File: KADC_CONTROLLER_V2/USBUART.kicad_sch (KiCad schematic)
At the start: 11 parts, among them J14 ZX62D-B-5P830, U10 PUSB3FR4Z, U9 FT230XQ-R

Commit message: many updates
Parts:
- added C159, C161, C174, C175, C176, C181, C182, C183, C184, C185, C26, C84, C86, C87: 0.1u, symbol Device:C_Small
- added C160, C177, C82, C83: 10u, symbol Device:C_Small
- added C186: 2.2u, symbol Device:C_Small
- added C2, C27, C3, C70, C71: 22u, symbol Device:C_Small
- added J1, J7: GSB311231HR, GSB311231HR_AMP, symbol GSB311231HR:GSB311231HR
- added R11: 12k, Resistor_SMD:R_0603_1608Metric, symbol Device:R_Small_US
- added R12, R13: 200k, Resistor_SMD:R_0603_1608Metric, symbol Device:R_Small_US
- added R159, R160: DNP, Resistor_SMD:R_0603_1608Metric, symbol Device:R_Small_US
- added R161, R163: 10k, Resistor_SMD:R_0603_1608Metric, symbol Device:R_Small_US
- added R162: 8.06k, Resistor_SMD:R_0603_1608Metric, symbol Device:R_Small_US
- added R8: 0R, Resistor_SMD:R_0603_1608Metric, symbol Device:R_Small_US
- added U16: USB3320C-EZK-TR, QFN32_5X5MC_MCH, symbol USB3320C_EZK_TR:USB3320C-EZK-TR
- added U17: USB5744/2G, VQFN56_2G_MCH, symbol USB4744:USB5744_2G
- added U33, U38: (no value), symbol MP62341:MP62341DH-LF-Z
- added U39, U40, U41, U42: TPD4S012DRYR, DRY6, symbol TPD4S012DRYR:TPD4S012DRYR
- added U46, U47, U48, U49: TPD4E05U06DQAR, DQA0010A, symbol TPD4E05U06DQAR:TPD4E05U06DQAR
- R31, R87: value R_US -> 27R
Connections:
- net GND: now also C160.2, C177.2, C185.1, C186.2, C2.2, C26.2, C27.2, C3.2, C70.2, C71.2, C82.2, C83.2, J1.13 (GND), J1.16 (GND_DRAIN), J1.4 (GND), J1.7 (GND_DRAIN), J7.13 (GND), J7.16 (GND_DRAIN), J7.4 (GND), J7.7 (GND_DRAIN), R11.2, R12.2, R13.2, R162.2, R8.2, U16.23 (ID), U16.33 (EPAD), U17.57 (VSS), U33.1 (GND), U38.1 (GND), U39.4 (GND), U40.4 (GND), U41.4 (GND), U42.4 (GND), U46.3 (GND), U46.8 (GND), U47.3 (GND), U47.8 (GND), U48.3 (GND), U48.8 (GND), U49.3 (GND), U49.8 (GND)
- net 1V8_Banks renamed PS_1V8
- net PS_1V8: now also U16.11 (REFSEL1), U16.14 (REFSEL2), U16.28 (VDD18), U16.30 (VDD18), U16.32 (VDDIO), U16.8 (REFSEL0)
- net 3V3_IO renamed PS_3V3
- net PS_3V3: now also R159.1, R160.1, R161.1, U17.16 (VDD33), U17.31 (VDD33), U17.37 (VBUS_DET), U17.44 (VDD33), U17.55 (VDD33)
- new net: C186.1, U16.20 (VDD33)
- new net: R163.2, U16.22 (VBUS)
- new net: R162.1, U16.24 (RBIAS)
- new net: R13.1, U17.40 (SPI_DI/CFG_BC_EN)
- new net: R12.1, U17.41 (SPI_CE_N/CFG_NON_REM)
- new net: R161.2, U17.42 (RESET_N)
- new net: C184.2, U17.47 (USB3UP_TXDP)
- new net: C183.2, U17.48 (USB3UP_TXDM)
- new net: C182.2, U17.50 (USB3UP_RXDP)
- new net: C181.2, U17.51 (USB3UP_RXDM)
- new net: R8.1, U17.52 (ATESET)
- new net: R11.1, U17.56 (RBIAS)
- new net 5V0_IN: C185.2, C2.1, C26.1, C27.1, C3.1, C70.1, C71.1, R163.1, U16.21 (VBAT), U33.2 (IN), U38.2 (IN)
- new net GTR_DP2_C2M_N: C183.1
- new net GTR_DP2_C2M_P: C184.1
- new net GTR_DP2_M2C_N: C181.1
- new net GTR_DP2_M2C_P: C182.1
- new net PS_1V2: U17.12 (VDD12), U17.15 (VDD12), U17.21 (VDD12), U17.28 (VDD12), U17.33 (VDD12), U17.43 (VDD12), U17.49 (VDD12), U17.5 (VDD12)
- new net USB0_CLK: U16.1 (CLKOUT)
- new net USB0_DATA0: U16.3 (DATA0)
- new net USB0_DATA1: U16.4 (DATA1)
- new net USB0_DATA2: U16.5 (DATA2)
- new net USB0_DATA3: U16.6 (DATA3)
- new net USB0_DATA5: U16.9 (DATA5)
- new net USB0_DATA6: U16.10 (DATA6)
- new net USB0_DATA7: U16.13 (DATA7), U16.7 (DATA4)
- new net USB0_DIR: U16.31 (DIR)
- new net USB0_NXT: U16.2 (NXT)
- new net USB0_STP: U16.29 (STP)
- new net USB3320_D_N: U16.19 (DM), U17.46 (USB2UP_DM)
- new net USB3320_D_P: U16.18 (DP), U17.45 (USB2UP_DP)
- new net USB_C_SSTX1+: C159.1, J1.18 (SSTX+), U48.1 (D1+), U48.10 (NC)
- new net USB_C_SSTX1-: C87.1, J1.17 (SSTX-), U48.2 (D1-), U48.9 (NC)
- new net USB_C_SSTX2+: C86.2, J1.9 (SSTX+), U48.4 (D2+), U48.7 (NC)
- new net USB_C_SSTX2-: C84.2, J1.8 (SSTX-), U48.5 (D2-), U48.6 (NC)
- new net USB_C_SSTX3+: C175.1, J7.18 (SSTX+), U46.1 (D1+), U46.10 (NC)
- new net USB_C_SSTX3-: C176.1, J7.17 (SSTX-), U46.2 (D1-), U46.9 (NC)
- new net USB_C_SSTX4+: C174.2, J7.9 (SSTX+), U46.4 (D2+), U46.7 (NC)
- new net USB_C_SSTX4-: C161.2, J7.8 (SSTX-), U46.5 (D2-), U46.6 (NC)
- new net USB_D1+: J1.12 (D+), U17.1 (USB2DN_DP1/PRT_DIS_P1), U39.1 (D+)
- new net USB_D1-: J1.11 (D-), U17.2 (USB2DN_DM1/PRT_DIS_M1), U39.2 (D-)
- new net USB_D2+: J1.3 (D+), U17.8 (USB2DN_DP2/PRT_DIS_P2), U40.1 (D+)
- new net USB_D2-: J1.2 (D-), U17.9 (USB2DN_DM2/PRT_DIS_M2), U40.2 (D-)
- new net USB_D3+: J7.12 (D+), U17.17 (USB2DN_DP3/PRT_DIS_P3), U41.1 (D+)
- new net USB_D3-: J7.11 (D-), U17.18 (USB2DN_DM3/PRT_DIS_M3), U41.2 (D-)
- new net USB_D4+: J7.3 (D+), U17.24 (USB2DN_DP4/PRT_DIS_P4), U42.1 (D+)
- new net USB_D4-: J7.2 (D-), U17.25 (USB2DN_DM4/PRT_DIS_M4), U42.2 (D-)
- new net USB_HUB_SMCLK: R160.2, U17.38 (SPI_CLK/SMCLK)
- new net USB_HUB_SMDAT: R159.2, U17.39 (SPI_DO/SMDAT)
- new net USB_PRT_CTRL1: U17.36 (PRT_CTL1), U33.3 (EN1), U33.8 (FLAG1_B)
- new net USB_PRT_CTRL2: U17.35 (PRT_CTL2), U33.4 (EN2), U33.5 (FLAG2_B)
- new net USB_PRT_CTRL3: U17.34 (PRT_CTL3), U38.3 (EN1), U38.8 (FLAG1_B)
- new net USB_PRT_CTRL4: U17.32 (PRT_CTL4/GANG_PWR), U38.4 (EN2), U38.5 (FLAG2_B)
- new net USB_SSRX1+: J1.15 (SSRX+), U17.6 (USB3DN_RXDP1), U49.1 (D1+), U49.10 (NC)
- new net USB_SSRX1-: J1.14 (SSRX-), U17.7 (USB3DN_RXDM1), U49.2 (D1-), U49.9 (NC)
- new net USB_SSRX2+: J1.6 (SSRX+), U17.13 (USB3DN_RXDP2), U49.4 (D2+), U49.7 (NC)
- new net USB_SSRX2-: J1.5 (SSRX-), U17.14 (USB3DN_RXDM2), U49.5 (D2-), U49.6 (NC)
- new net USB_SSRX3+: J7.15 (SSRX+), U17.22 (USB3DN_RXDP3), U47.1 (D1+), U47.10 (NC)
- new net USB_SSRX3-: J7.14 (SSRX-), U17.23 (USB3DN_RXDM3), U47.2 (D1-), U47.9 (NC)
- new net USB_SSRX4+: J7.6 (SSRX+), U17.29 (USB3DN_RXDP4), U47.4 (D2+), U47.7 (NC)
- new net USB_SSRX4-: J7.5 (SSRX-), U17.30 (USB3DN_RXDM4), U47.5 (D2-), U47.6 (NC)
- new net USB_SSTX1+: C159.2, U17.3 (USB3DN_TXDP1)
- new net USB_SSTX1-: C87.2, U17.4 (USB3DN_TXDM1)
- new net USB_SSTX2+: C86.1, U17.10 (USB3DN_TXDP2)
- new net USB_SSTX2-: C84.1, U17.11 (USB3DN_TXDM2)
- new net USB_SSTX3+: C175.2, U17.19 (USB3DN_TXDP3)
- new net USB_SSTX3-: C176.2, U17.20 (USB3DN_TXDM3)
- new net USB_SSTX4+: C174.1, U17.26 (USB3DN_TXDP4)
- new net USB_SSTX4-: C161.1, U17.27 (USB3DN_TXDM4)
- new net USB_VBUS1: C82.1, J1.10 (VBUS), U33.7 (OUT1), U39.6 (Vbus)
- new net USB_VBUS2: C83.1, J1.1 (VBUS), U33. (OUT2), U40.6 (Vbus)
- new net USB_VBUS3: C177.1, J7.10 (VBUS), U38.7 (OUT1), U41.6 (Vbus)
- new net USB_VBUS4: C160.1, J7.1 (VBUS), U38. (OUT2), U42.6 (Vbus)
- no-connect marks 8 -> 17
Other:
- note added: "(3)"
- note added: "(8)"
- note added: "UART (Via USB)"
- note added: "USB CONNECTORS 1-2"
- note added: "USB CONNECTORS 3-4"
- moved on the sheet: C107, C65, C66, C68, C69, J14, R31, R81, R87, U10, U9

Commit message: More Things
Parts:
- added C243: 22p, symbol Device:C_Small
- added Q10: DMN2310U-7, Package_TO_SOT_SMD:TSOT-23, symbol Simulation_SPICE:NMOS
- added R115, R203: DNP, Resistor_SMD:R_0603_1608Metric, symbol Device:R_Small_US
- added R204: 10k, Resistor_SMD:R_0603_1608Metric, symbol Device:R_Small_US
- added R205: 3.01k, Resistor_SMD:R_0603_1608Metric, symbol Device:R_Small_US
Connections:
- net GND: now also C243.2, R203.2
- net PS_1V8: now also Q10.2 (G), R204.1
- net PS_3V3: now also R115.2, R205.1
- net USB_PHY_REFCLK: now reaches U16.26 (REFCLK)
- net PS_POR: now reaches U16.27 (RESETB)
- net PS_POR: now also Q10.3 (S), R204.2
- net at R161.2, U17.42 (RESET_N): now also C243.1, Q10.1 (D), R205.2
- net USB_HUB_CLK_IN: now reaches U17.54 (XTALI/CLK_IN)
- net USB_HUB_CLK_IN: now also R115.1, R203.1

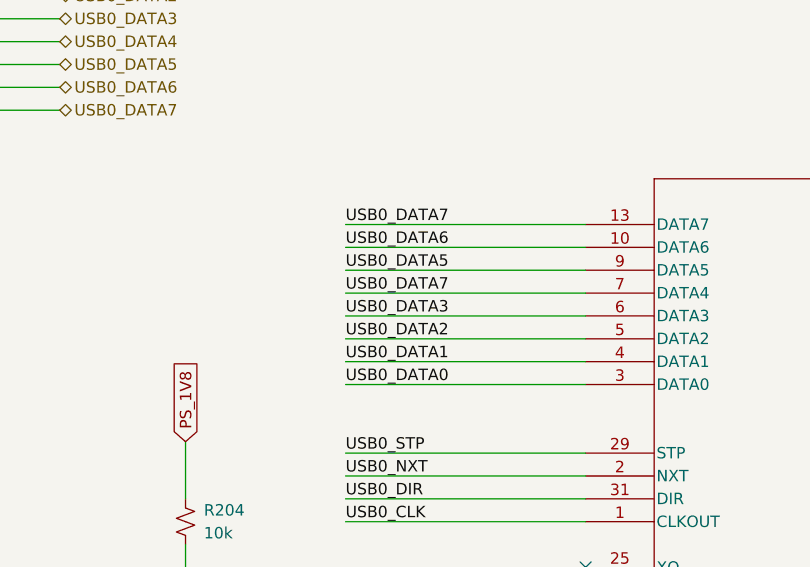
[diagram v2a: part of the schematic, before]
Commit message: Added footprints, updated schematic
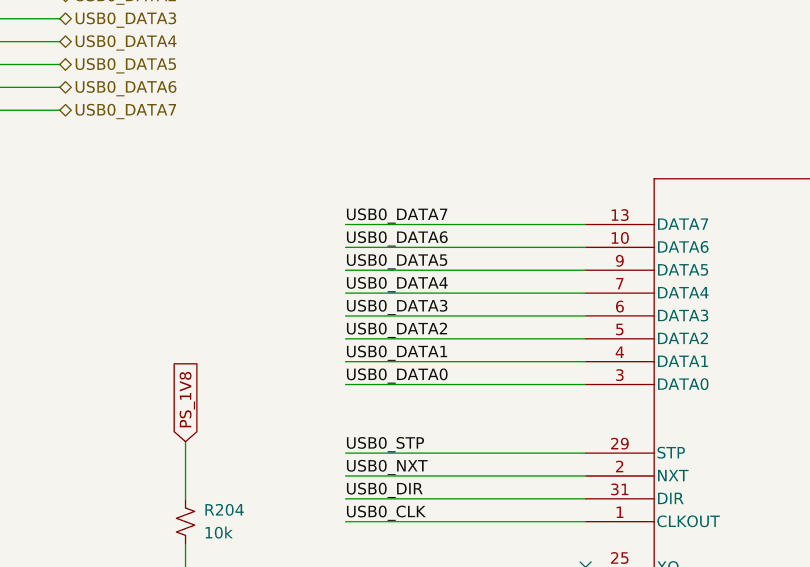
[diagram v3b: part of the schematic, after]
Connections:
- net USB0_DATA4: now also U16.7 (DATA4)
- net USB0_DATA7: no longer U16.7 (DATA4)
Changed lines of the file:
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@@
 		)
 	)
-	(label "USB0_DATA7"
+	(label "USB0_DATA4"
 		(at 378.46 60.96 0)
 		(effects

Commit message: Quick Updates, Power verification finalized
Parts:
- J1, J7: footprint GSB311231HR_AMP -> GSB31123HR:GSB311231HR_AMP
- J14: footprint ZX62D_B_5P8_30_:ZX62D-B-5P830_HIR -> ZX62D_B_5P8_30:ZX62D-B-5P830_HIR
- U16: footprint QFN32_5X5MC_MCH -> USB3320C_EZK_TR:QFN32_5X5MC_MCH
- U33, U38: value (none) -> MP62341DH-LF-Z
- U39, U40, U41, U42: footprint DRY6 -> TPD4S012DRYR:DRY6
- U46, U47, U48, U49: footprint DQA0010A -> TPD4E05U06DQAR:DQA0010A
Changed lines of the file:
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@@
 			)
 		)
-		(property "Footprint" "QFN32_5X5MC_MCH"
+		(property "Footprint" "USB3320C_EZK_TR:QFN32_5X5MC_MCH"
 			(at 442.976 37.084 0)
 			(hide yes)
@@
 			)
 		)
-		(property "Footprint" "DRY6"
+		(property "Footprint" "TPD4S012DRYR:DRY6"
 			(at 402.59 367.03 0)
 			(hide yes)
@@
 		(in_pos_files yes)
 		(dnp no)
-		(fields_autoplaced yes)
 		(property "Reference" "U33"
 			(at 286.004 325.12 0)
-			(hide yes)
 			(show_name no)
 			(do_not_autoplace no)
@@
 			)
 		)
-		(property "Value" ""
-			(at 283.21 335.28 0)
+		(property "Value" "MP62341DH-LF-Z"
+			(at 286.512 328.676 0)
 			(show_name no)
 			(do_not_autoplace no)
@@
 			)
 		)
-		(property "Footprint" "DQA0010A"
+		(property "Footprint" "TPD4E05U06DQAR:DQA0010A"
 			(at 194.31 228.346 0)
 			(hide yes)
@@
 			)
 		)
-		(property "Footprint" "GSB311231HR_AMP"
+		(property "Footprint" "GSB31123HR:GSB311231HR_AMP"
 			(at 77.47 243.078 0)
 			(hide yes)
@@
 			)
 		)
-		(property "Footprint" "DQA0010A"
+		(property "Footprint" "TPD4E05U06DQAR:DQA0010A"
 			(at 194.31 136.906 0)
 			(hide yes)
@@
 			)
 		)
-		(property "Footprint" "GSB311231HR_AMP"
+		(property "Footprint" "GSB31123HR:GSB311231HR_AMP"
 			(at 73.66 147.828 0)
 			(hide yes)
@@
 			)
 		)
-		(property "Footprint" "DRY6"
+		(property "Footprint" "TPD4S012DRYR:DRY6"
 			(at 402.59 389.89 0)
 			(hide yes)
@@
 			)
 		)
-		(property "Footprint" "DRY6"
+		(property "Footprint" "TPD4S012DRYR:DRY6"
 			(at 402.59 344.17 0)
 			(hide yes)
@@
 		(in_pos_files yes)
 		(dnp no)
-		(fields_autoplaced yes)
 		(property "Reference" "U38"
 			(at 287.274 365.76 0)
-			(hide yes)
 			(show_name no)
 			(do_not_autoplace no)
@@
 			)
 		)
-		(property "Value" ""
-			(at 284.48 375.92 0)
+		(property "Value" "MP62341DH-LF-Z"
+			(at 287.02 369.062 0)
 			(show_name no)
 			(do_not_autoplace no)
@@
 			)
 		)
-		(property "Footprint" "DRY6"
+		(property "Footprint" "TPD4S012DRYR:DRY6"
 			(at 402.59 323.85 0)
 			(hide yes)
@@
 			)
 		)
-		(property "Footprint" "DQA0010A"
+		(property "Footprint" "TPD4E05U06DQAR:DQA0010A"
 			(at 194.31 271.526 0)
 			(hide yes)
@@
 			)
 		)
-		(property "Footprint" "DQA0010A"
+		(property "Footprint" "TPD4E05U06DQAR:DQA0010A"
 			(at 194.31 183.896 0)
 			(hide yes)
@@
 			)
 		)
-		(property "Footprint" "ZX62D_B_5P8_30_:ZX62D-B-5P830_HIR"
+		(property "Footprint" "ZX62D_B_5P8_30:ZX62D-B-5P830_HIR"
 			(at 211.074 26.67 0)
 			(hide yes)

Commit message: Reupdate for verify
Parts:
- U17: footprint VQFN56_2G_MCH -> USB5744_2G:VQFN56_2G_MCH
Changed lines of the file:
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@@
 			)
 		)
-		(property "Footprint" "VQFN56_2G_MCH"
+		(property "Footprint" "USB5744_2G:VQFN56_2G_MCH"
 			(at 439.42 138.684 0)
 			(hide yes)

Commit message: update
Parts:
- added C67, C72: 100n, Capacitor_SMD:C_0603_1608Metric, symbol Device:C
- added R65: 4.7k, Resistor_SMD:R_0603_1608Metric, symbol Device:R_US
- added R69: 10k, Resistor_SMD:R_0603_1608Metric, symbol Device:R_US
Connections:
- net GND: now also C67.2, C72.2, R69.1
- net PS_3V3: now also C67.1, C72.1
- net UART_VSENSE: now reaches U9.12 (CBUS0)
- net UART_VSENSE: now also R65.1, R69.2
- net at J14.1: now also R65.2
- no-connect marks 17 -> 15
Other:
- note added: "FT230X SELF-POWERED USB CONFIGURATION USB VBUS SENSE: J14.1 VBUS -> 4.7k -> USB_VBUS_SENSE -> U9.12 CBUS0 USB_VBUS_SENSE -> 10k -> GND U9 CBUS0 SHALL BE PROGRAMMED AS "VBUS_Sense" USING FTDI FT_PROG VIA THE NORMAL USB INTERFACE. FT230X MTP SETTINGS: - POWER SOURCE = SELF POWERED - MAX BUS POWER = 0mA - CBUS0 = VBUS_Sense - USB SUSPEND VBUS = ENABLED PROGRAMMING OCCURS OVER U9 USBDP/USBDM THROUGH 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"
- moved on the sheet: C107, C159, C160, C161, C174, C175, C176, C177, C181, C182, C183, C184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

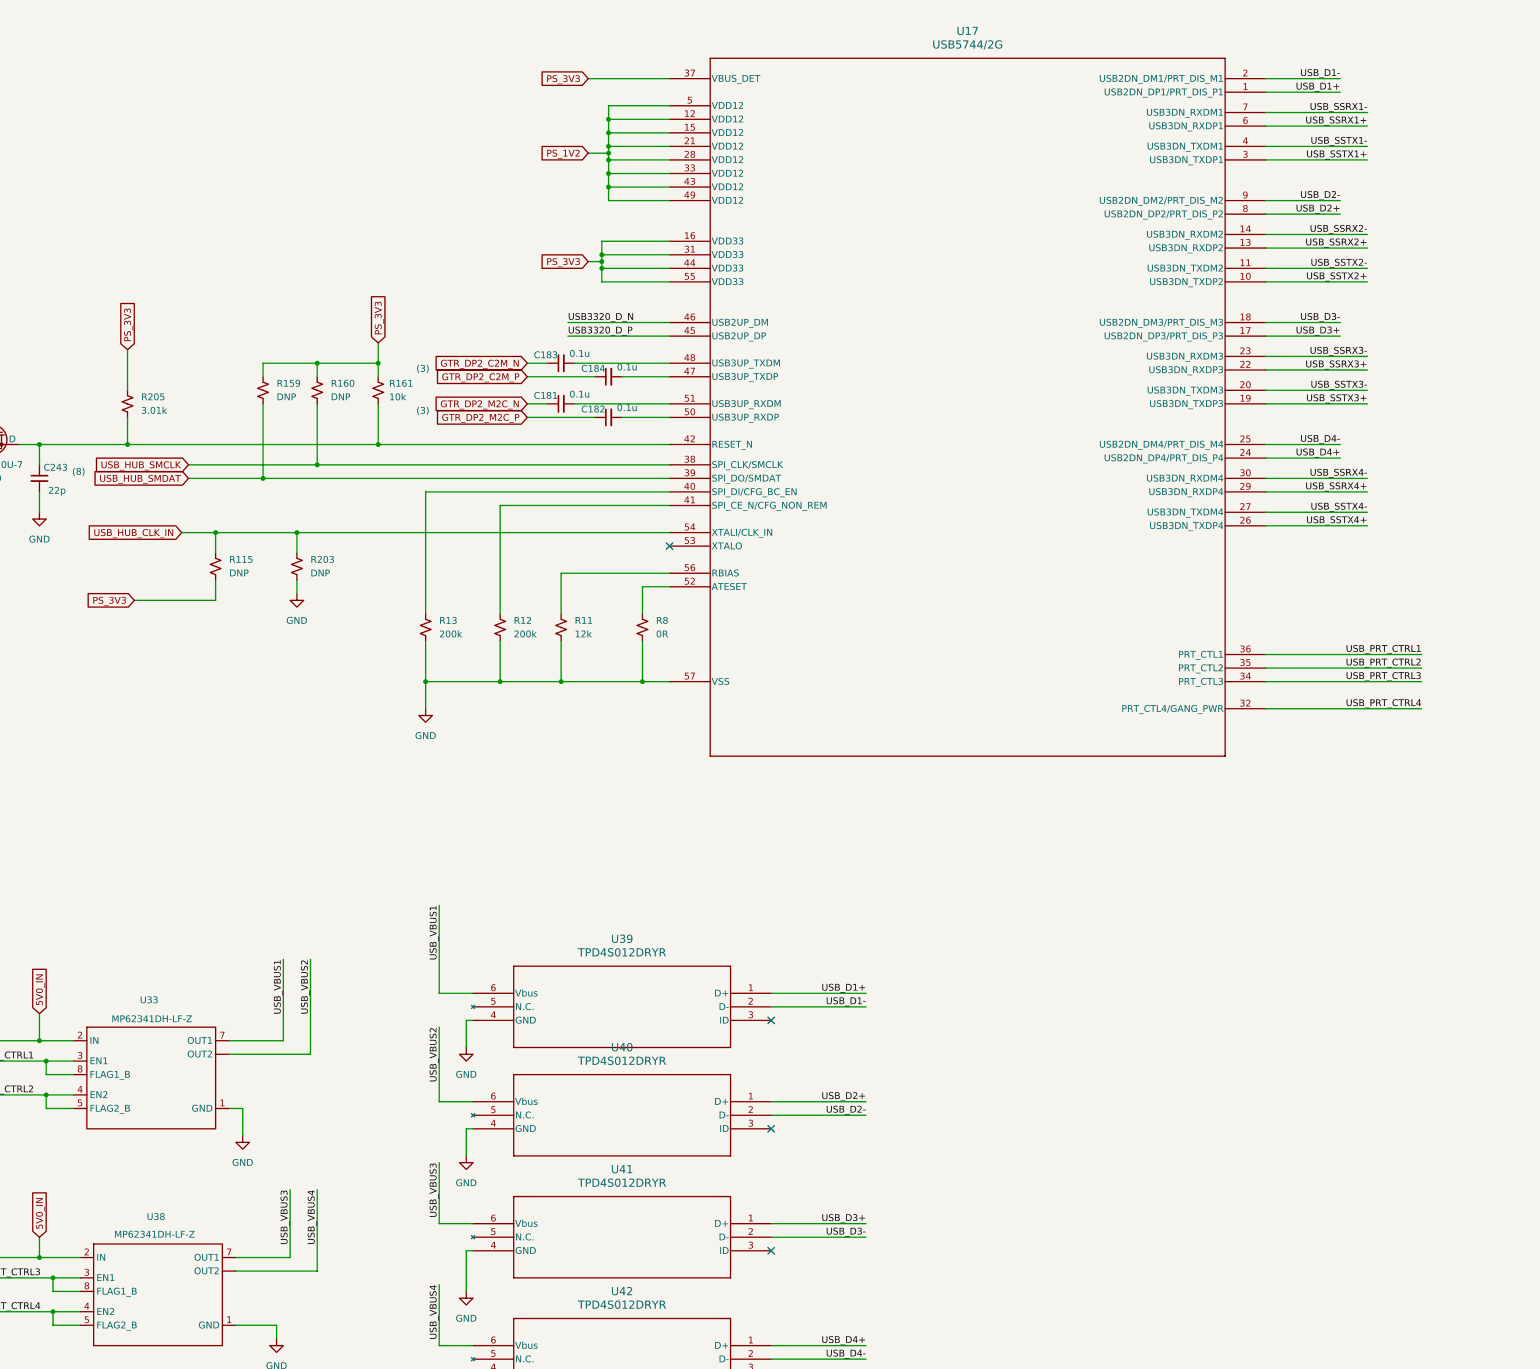
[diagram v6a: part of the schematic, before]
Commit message: updated sd symbol
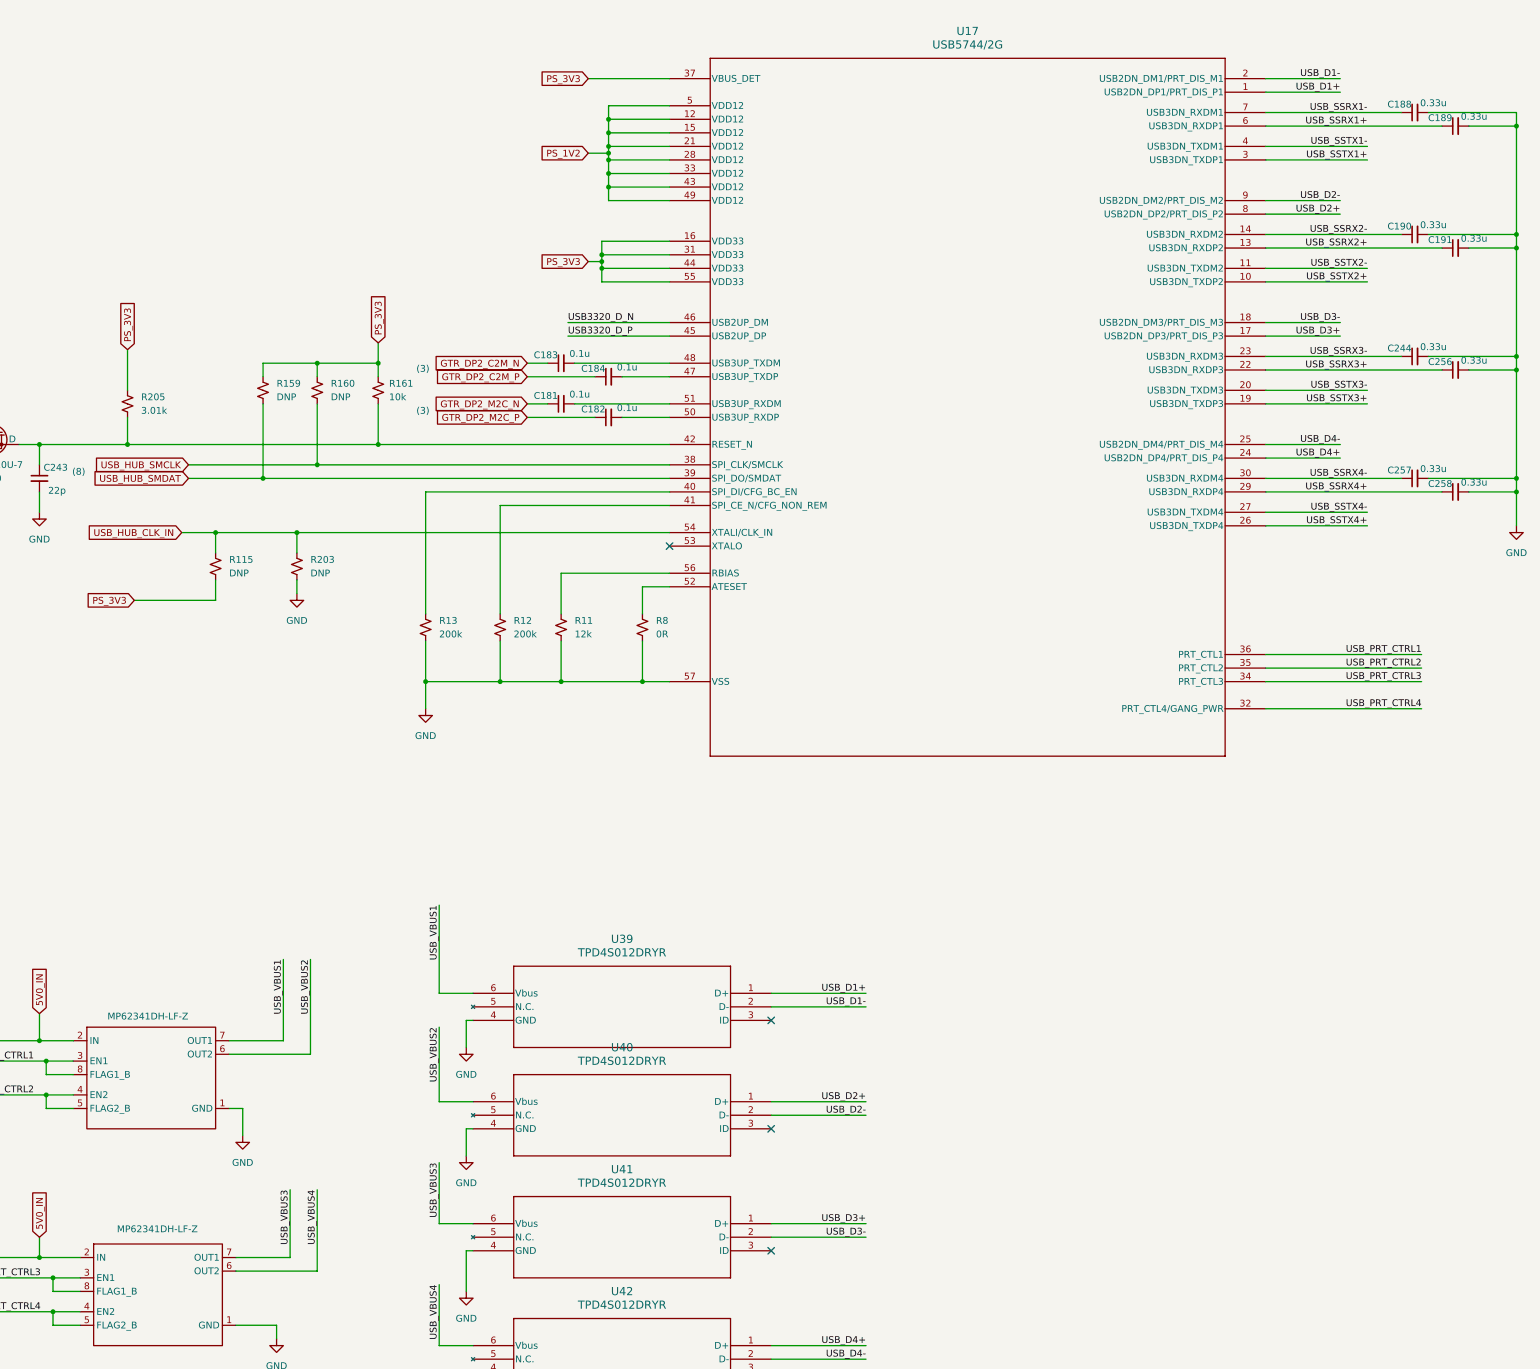
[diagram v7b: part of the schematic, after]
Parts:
- removed U33, U38: MP62341DH-LF-Z, symbol MP62341:MP62341DH-LF-Z
- added C188, C189, C190, C191, C244, C256, C257, C258: 0.33u, symbol Device:C_Small
- added U22, U23: MP62341DH-LF-Z, symbol MP62341:MP62341DH-LF-Z
- C184, C186: footprint (none) -> Capacitor_SMD:C_0603_1608Metric
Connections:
- net 5V0_IN: now also U22.2 (IN), U23.2 (IN)
- net GND: now also C188.2, C189.2, C190.2, C191.2, C244.2, C256.2, C257.2, C258.2, U22.1 (GND), U23.1 (GND)
- net USB_PRT_CTRL1: now also U22.3 (EN1), U22.8 (FLAG1_B)
- net USB_PRT_CTRL2: now also U22.4 (EN2), U22.5 (FLAG2_B)
- net USB_PRT_CTRL3: now also U23.3 (EN1), U23.8 (FLAG1_B)
- net USB_PRT_CTRL4: now also U23.4 (EN2), U23.5 (FLAG2_B)
- net USB_SSRX1+: now also C189.1
- net USB_SSRX1-: now also C188.1
- net USB_SSRX2+: now also C191.1
- net USB_SSRX2-: now also C190.1
- net USB_SSRX3+: now also C256.1
- net USB_SSRX3-: now also C244.1
- net USB_SSRX4+: now also C258.1
- net USB_SSRX4-: now also C257.1
- net USB_VBUS1: now also U22.7 (OUT1)
- net USB_VBUS2: now also U22.6 (OUT2)
- net USB_VBUS3: now also U23.7 (OUT1)
- net USB_VBUS4: now also U23.6 (OUT2)
